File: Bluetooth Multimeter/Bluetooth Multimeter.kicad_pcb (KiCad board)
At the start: 2 copper layers, 55 x 90 mm, 33 parts, among them J1 V/Ohm, J2 Com, J3 mA, J4 A, J5 Parallel Prot, J6 3.3V, J7 GND, K1 Low Range, K2 Medium Range, K3 High Range, K4 UH Range (Ohm Only), K5 V/Ohm Switch, U1 ItsyBitsy_NRF52840_Big

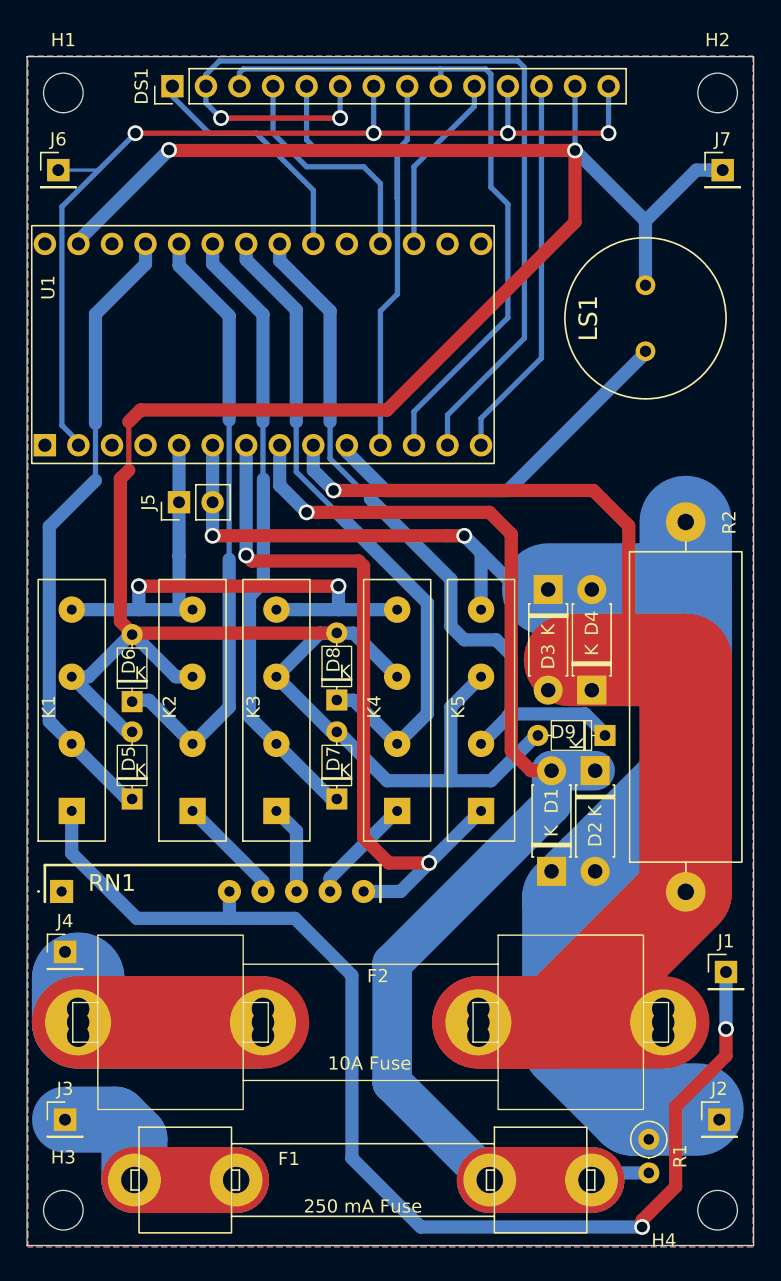
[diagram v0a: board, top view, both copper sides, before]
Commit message: made inverted connector PCB main project, fixed ohmeter
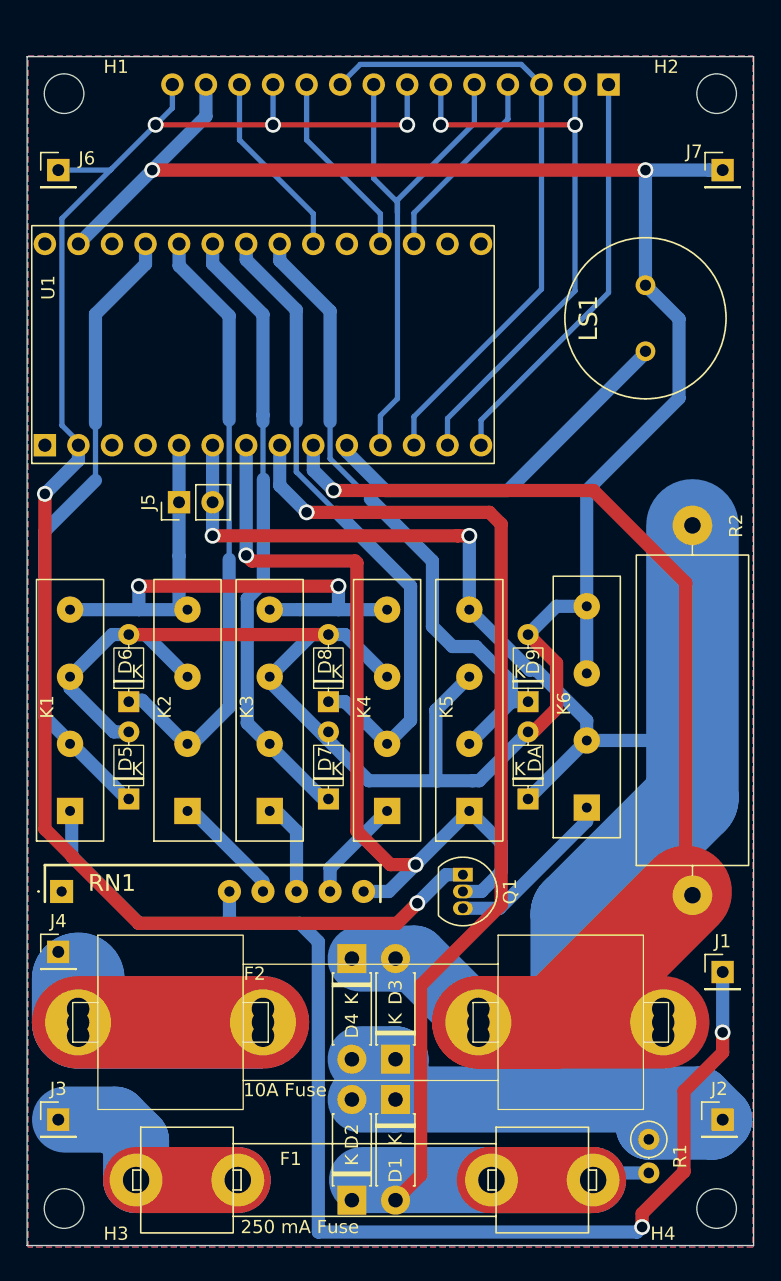
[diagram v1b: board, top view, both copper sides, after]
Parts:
- added DA: 1N4148, 502ProjectFootprints:D_DO-35_SOD27_P5.08mm_Horizontal, F.Cu at (158.2, 109.6)
- added K6: Ohm Common GND, 502ProjectFootprints:SIL03-1A72-71_4, F.Cu at (162.7, 102.6)
- added Q1: 2N7000, Package_TO_SOT_THT:TO-92_Inline, F.Cu at (153.3, 115.3)
- DS1: moved to B.Cu
- moved D3 37.4 mm to (148.2, 129.3), turned to 90 degrees
- moved D2 37.4 mm to (144.9, 140.0), turned to 90 degrees
- moved DS1 33.0 mm to (164.3, 55.5)
- moved D4 27.3 mm to (144.9, 121.7), turned to -90 degrees
- moved D1 20.9 mm to (148.2, 132.3), turned to -90 degrees
- moved D9 6.36 mm to (158.2, 102.2), turned to 90 degrees
- moved K5 0.89 mm to (153.8, 102.9)
- moved K4 0.76 mm to (147.6, 102.9)
- moved D8 0.65 mm to (143.1, 102.2)
- moved D7 0.64 mm to (143.1, 109.6)
- moved R2 0.57 mm to (170.7, 102.9)
- moved K3 0.51 mm to (138.7, 102.9)
- moved J3 0.51 mm to (122.7, 133.9)
- moved J4 0.51 mm to (122.7, 121.2)
- moved K2 0.38 mm to (132.5, 102.9)
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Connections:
- U1 pad 14: /TFT CS -> /TOUCH IRQ
- U1 pad 17: /TFT DC -> /TOUCH CS
- U1 pad 18: /TOUCH CS -> /TFT DC
- U1 pad 20: /TOUCH IRQ -> /TFT CS
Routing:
- net +3.3V: track 73.4 -> 126.5 mm, vias 4 -> 5
- net /Input Common: track 114.0 -> 150.0 mm
- net /MISO: track 70.7 -> 44.5 mm
- net GND: track 210.6 -> 194.0 mm
- net /mA ADC In: track 107.7 -> 123.4 mm
- net /TOUCH IRQ: track 17.4 -> 31.3 mm
- net /TFT CS: track 28.1 -> 14.4 mm
- net Net-(K6-COM): track 0.00 -> 13.1 mm
- net /V/Ohm Control: track 57.7 -> 50.3 mm
- net /Ohm Vout: track 55.3 -> 62.4 mm
- net /MOSI: track 52.9 -> 47.8 mm
- net /V/Ohm In: track 90.2 -> 95.3 mm
- net /A ADC In: track 99.9 -> 104.7 mm
- net /TOUCH CS: track 17.8 -> 15.0 mm
- net /TFT DC: track 12.8 -> 14.4 mm
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
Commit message: rerouted board for external fab
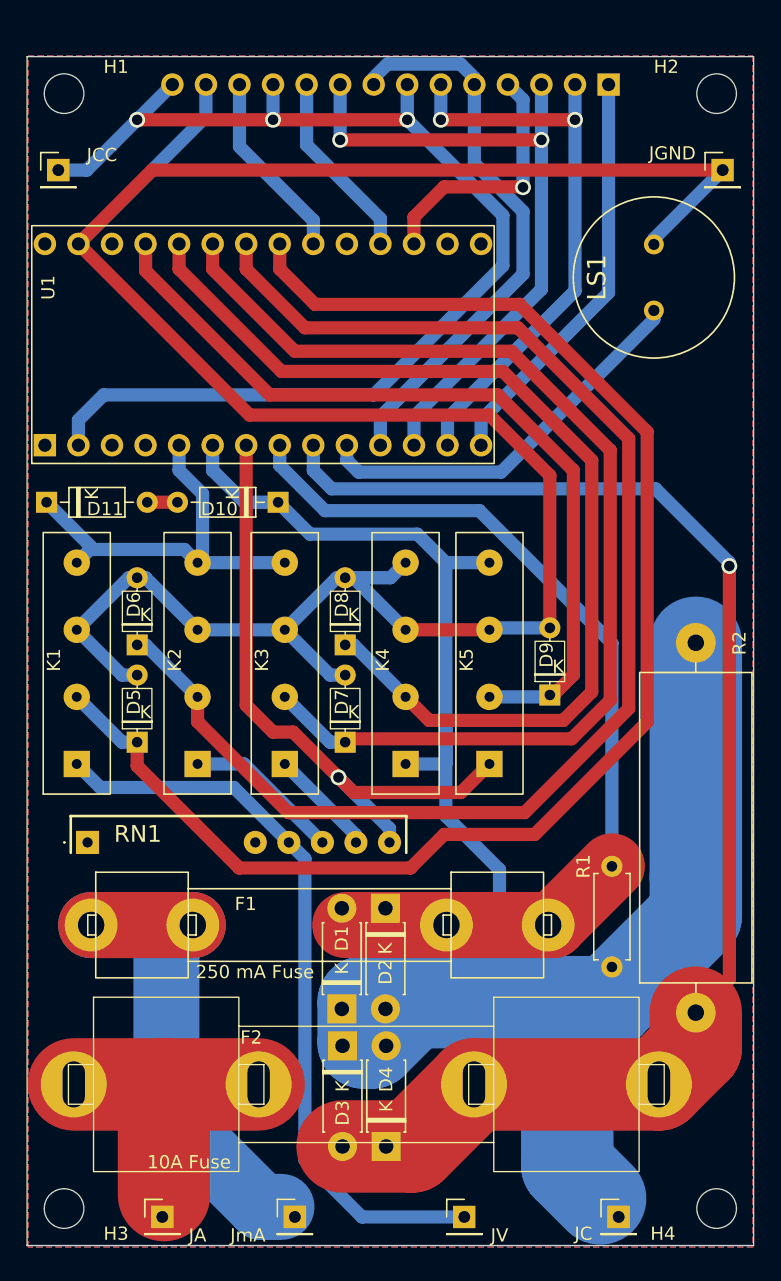
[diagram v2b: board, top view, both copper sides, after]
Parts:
- removed DA: 1N4148, 502ProjectFootprints:D_DO-35_SOD27_P5.08mm_Horizontal
- removed J1: V/Ohm, 502ProjectFootprints:PinHeader_1x01_P2.54mm_Vertical_H0.9mm
- removed J2: Com, 502ProjectFootprints:PinHeader_1x01_P2.54mm_Vertical_H0.9mm
- removed J3: mA, 502ProjectFootprints:PinHeader_1x01_P2.54mm_Vertical_H0.9mm
- removed J4: A, 502ProjectFootprints:PinHeader_1x01_P2.54mm_Vertical_H0.9mm
- removed J5: Parallel Prot, 502ProjectFootprints:PinHeader_1x02_P2.54mm_Vertical_H0.9mm
- removed K6: Ohm Common GND, 502ProjectFootprints:SIL03-1A72-71_4
- removed Q1: 2N7000, Package_TO_SOT_THT:TO-92_Inline
- added D10: D_Zener, Diode_THT:D_DO-35_SOD27_P7.62mm_Horizontal, F.Cu at (139.3, 87.1)
- added D11: D_Zener, Diode_THT:D_DO-35_SOD27_P7.62mm_Horizontal, F.Cu at (121.8, 87.1)
- added JA: A, 502ProjectFootprints:PinHeader_1x01_P2.54mm_Vertical_H0.9mm, F.Cu at (130.6, 141.2)
- added JC: Com, 502ProjectFootprints:PinHeader_1x01_P2.54mm_Vertical_H0.9mm, F.Cu at (165.1, 141.2)
- added JV: V/Ohm, 502ProjectFootprints:PinHeader_1x01_P2.54mm_Vertical_H0.9mm, F.Cu at (153.4, 141.2)
- added JmA: mA, 502ProjectFootprints:PinHeader_1x01_P2.54mm_Vertical_H0.9mm, F.Cu at (140.6, 141.2)
- F1: footprint 502ProjectFootprints:LF124061_3 -> 502ProjectFootprints:LF124061_4
- F2: footprint 502ProjectFootprints:LF124041_6 -> 502ProjectFootprints:LF124041_7
- K4: value UH Range (Ohm Only) -> Ohm Gnd
- R1: footprint Resistor_THT:R_Axial_DIN0207_L6.3mm_D2.5mm_P2.54mm_Vertical -> Resistor_THT:R_Axial_DIN0207_L6.3mm_D2.5mm_P7.62mm_Horizontal
- moved D2 22.2 mm to (147.4, 117.9), turned to -90 degrees
- moved F1 19.6 mm to (132.9, 119.1)
- moved D4 14.5 mm to (147.5, 135.9), turned to 90 degrees
- moved R1 13.3 mm to (164.6, 122.3), turned to 90 degrees
- moved R2 8.89 mm to (170.9, 111.8)
- moved D1 7.97 mm to (144.1, 125.5), turned to 90 degrees
- moved F2 4.71 mm to (154.1, 131.2)
- moved D7 4.48 mm to (144.4, 105.3)
- moved D8 4.48 mm to (144.4, 97.9)
- moved D5 4.35 mm to (128.7, 105.3)
- moved D6 4.35 mm to (128.7, 97.9)
- moved RN1 4.20 mm to (124.9, 112.9)
- moved D3 4.14 mm to (144.2, 128.3), turned to -90 degrees
- moved K5 3.87 mm to (155.3, 99.3)
- moved K4 3.82 mm to (149.0, 99.3)
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- renumbered J6 to JCC, J7 to JGND
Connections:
- D8 pad 1: /UH Range Control -> /Ohm Gnd Control
- K4 pad 1: Net-(K4-COM) -> /Input Common
- K4 pad 3: /UH Range Control -> /Ohm Gnd Control
- K4 pad 7: /V/Ohm ADC In -> GND
- RN1 pad 2: /V/Ohm In -> unconnected-(RN1-900k-Pad2)
- RN1 pad 3: Net-(K2-COM) -> /V/Ohm In
- RN1 pad 4: Net-(K3-COM) -> Net-(K2-COM)
- RN1 pad 5: Net-(K4-COM) -> Net-(K3-COM)
- U1 pad 21: /V/Ohm Control -> /Low Range Control
- U1 pad 22: /UH Range Control -> /Med Range Control
- U1 pad 24: /Med Range Control -> /Ohm Gnd Control
- U1 pad 25: /Low Range Control -> /V/Ohm Control
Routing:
- net /Ohm Gnd Control: track 0.00 -> 78.6 mm
- net /UH Range Control: track 64.8 -> 0.00 mm
- net /Low Range Control: track 49.4 -> 111.0 mm
- net /Med Range Control: track 48.6 -> 103.5 mm
- net /mA ADC In: track 123.4 -> 71.2 mm, vias 1 -> 0
- net /V/Ohm In: track 95.3 -> 56.9 mm, vias 2 -> 0
- net +3.3V: track 126.5 -> 90.0 mm, vias 5 -> 3
- net /High Range Control: track 48.1 -> 84.0 mm
- net /V/Ohm ADC In: track 53.2 -> 31.3 mm, vias 2 -> 0
- net /mA In: track 24.4 -> 41.5 mm
- net /Ohm Vout: track 62.4 -> 48.3 mm, vias 2 -> 1
- net Net-(K6-COM): track 13.1 -> 0.00 mm
- net /V/Ohm Control: track 50.3 -> 63.2 mm
- net /Input Common: track 150.0 -> 139.2 mm, vias 2 -> 0
- net /A In: track 31.3 -> 22.4 mm
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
